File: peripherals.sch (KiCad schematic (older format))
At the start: 61 parts, among them J12 U_FL-R-SMT-1_10_, J5 U_FL-R-SMT-1_10_, J6 U_FL-R-SMT-1_10_, J7 DM3AT-SF-PEJM5, J8 693022010811, U10 NCP163ASN330T1G, U11 EMIF06-MSD02N16

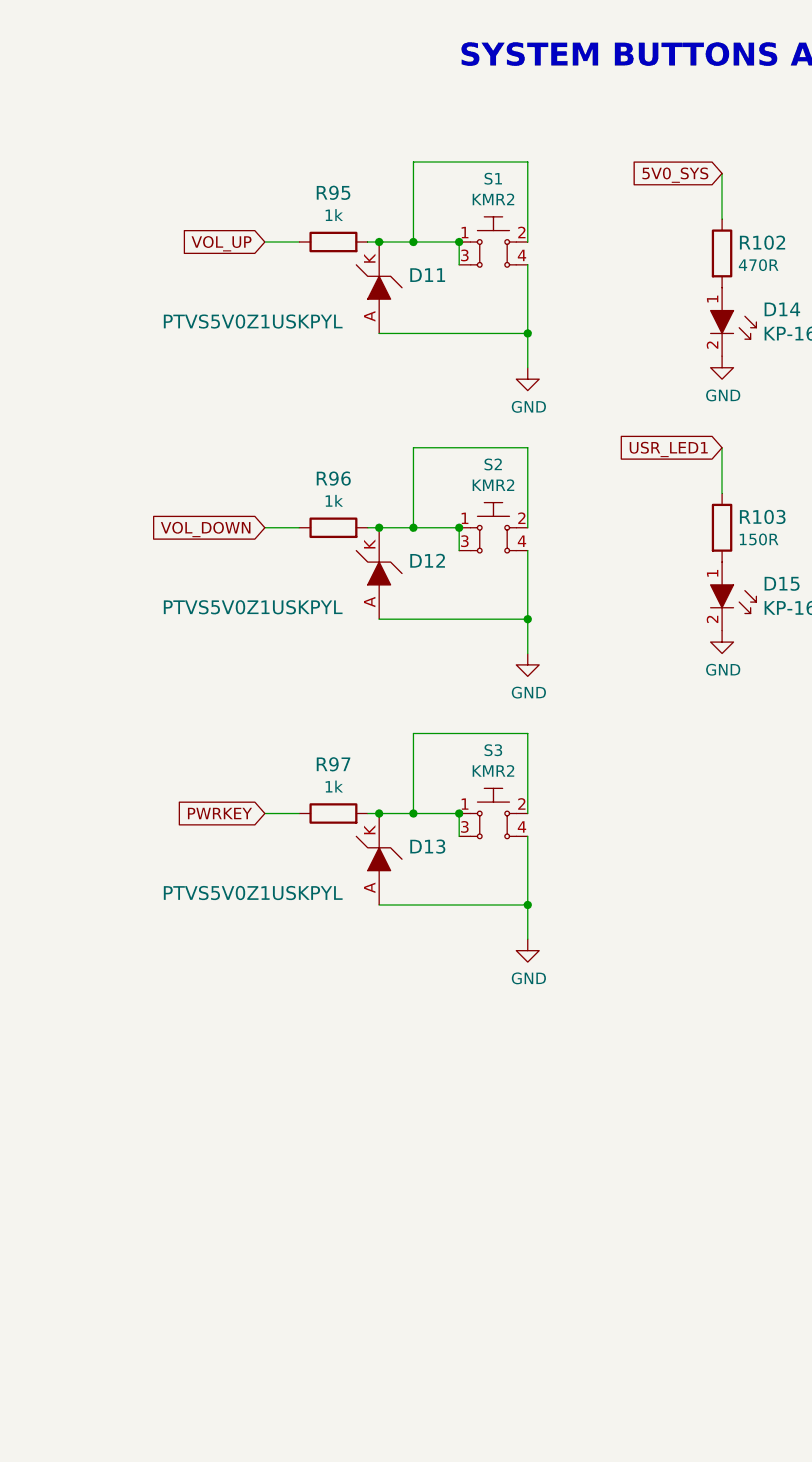
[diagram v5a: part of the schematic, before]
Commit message: Added USB BOOT, placed USR LEDs and buttons, connected Test Points
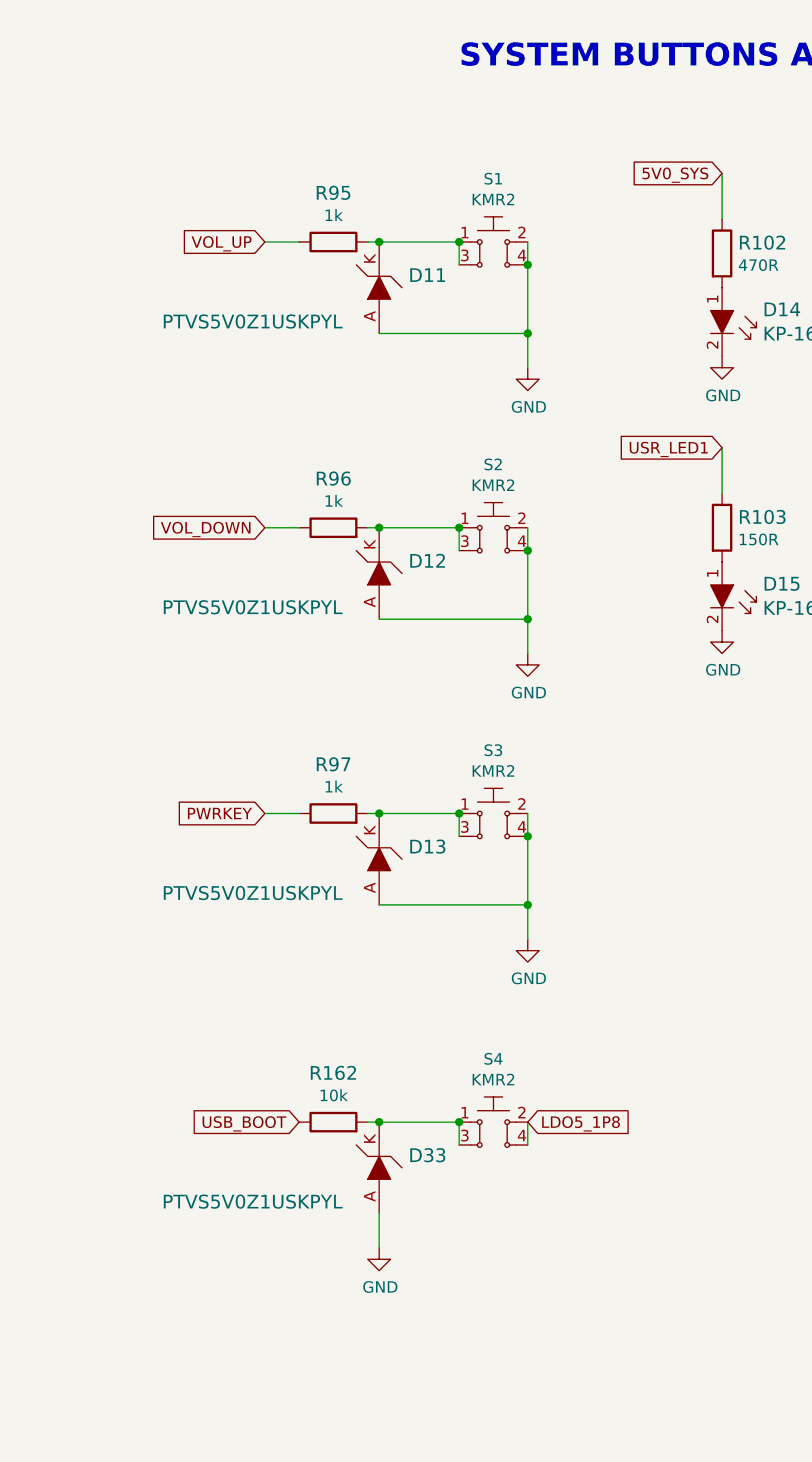
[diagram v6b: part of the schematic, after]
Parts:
- added D33: PTVS5V0Z1USKPYL, sc606-baseboard-footprints:SOD-964, symbol sc606-baseboard:PTVS5V0Z1USKPYL
- added R162: R_10k_0402, antmicro-footprints:0402-res, symbol antmicroResistors0402:R_10k_0402
- added S4: KMR2, sc606-baseboard-footprints:SW_SPST_4.2x2.8, symbol sc606-baseboard:KMR2
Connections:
- net GND: now also S1.2, S2.2, S3.2, D33.A
- net at D11.K, R95.2, S1.1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: no longer S1.2
- net at D12.K, R96.2, S2.1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: no longer S2.2
- net at D13.K, R97.2, S3.1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: no longer S3.2
- new net: D33.K, R162.2, S4.1, S4.3
- new net LDO5_1P8: S4.2, S4.4
- new net USB_BOOT: R162.1
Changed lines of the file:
@@
 VOL_UP
-$Comp
-L sc606-baseboard:KMR2 S1
-U 1 1 61E6F39D
-P 7950 5150
-F 0 "S1" H 7950 5425 50  0000 C CNN
-F 1 "KMR2" H 7950 5334 50  0000 C CNN
-F 2 "sc606-baseboard-footprints:SW_SPST_4.2x2.8" H 8150 5350 50  0001 L CNN
-F 3 "http://www.farnell.com/datasheets/2631211.pdf" H 8150 5450 60  0001 L CNN
-F 4 "KMR211NGLFS" H 8146 5543 60  0001 L CNN "MPN"
-F 5 "C&K Components" H 8150 5622 60  0001 L CNN "Manufacturer"
-	1    7950 5150
-	1    0    0    -1
-$EndComp
 $Comp
 L sc606-baseboard:GND-power #PWR0104
@@
 	1    0    0    -1
 $EndComp
-Wire Wire Line
-	7800 5150 7600 5150
-Wire Wire Line
-	8100 5150 8100 4800
-Wire Wire Line
-	8100 4800 7600 4800
-Wire Wire Line
-	7600 4800 7600 5150
-Connection ~ 7600 5150
-Wire Wire Line
-	7600 5150 7450 5150
 $Comp
 L sc606-baseboard:R_1k_0402 R95
@@
 	1    0    0    -1
 $EndComp
-Wire Wire Line
-	7800 6400 7600 6400
-Wire Wire Line
-	8100 6400 8100 6050
-Wire Wire Line
-	8100 6050 7600 6050
-Wire Wire Line
-	7600 6050 7600 6400
-Connection ~ 7600 6400
-Wire Wire Line
-	7600 6400 7450 6400
 $Comp
 L sc606-baseboard:R_1k_0402 R96
@@
 	1    0    0    -1
 $EndComp
-Wire Wire Line
-	7800 7650 7600 7650
-Wire Wire Line
-	8100 7650 8100 7300
-Wire Wire Line
-	8100 7300 7600 7300
-Wire Wire Line
-	7600 7300 7600 7650
-Connection ~ 7600 7650
-Wire Wire Line
-	7600 7650 7450 7650
 $Comp
 L sc606-baseboard:R_1k_0402 R97
@@
 Wire Wire Line
 	2600 8350 2600 8150
+Wire Wire Line
+	7450 5150 7800 5150
+$Comp
+L sc606-baseboard:KMR2 S1
+U 1 1 61E6F39D
+P 7950 5150
+F 0 "S1" H 7950 5425 50  0000 C CNN
+F 1 "KMR2" H 7950 5334 50  0000 C CNN
+F 2 "sc606-baseboard-footprints:SW_SPST_4.2x2.8" H 8150 5350 50  0001 L CNN
+F 3 "http://www.farnell.com/datasheets/2631211.pdf" H 8150 5450 60  0001 L CNN
+F 4 "KMR211NGLFS" H 8146 5543 60  0001 L CNN "MPN"
+F 5 "C&K Components" H 8150 5622 60  0001 L CNN "Manufacturer"
+	1    7950 5150
+	1    0    0    -1
+$EndComp
+Wire Wire Line
+	8100 5150 8100 5250
+Connection ~ 8100 5250
+Wire Wire Line
+	8100 6400 8100 6500
+Connection ~ 8100 6500
+Wire Wire Line
+	8100 7650 8100 7750
+Connection ~ 8100 7750
+Wire Wire Line
+	7450 7650 7800 7650
+Wire Wire Line
+	7450 6400 7800 6400
+$Comp
+L sc606-baseboard:KMR2 S4
+U 1 1 622633BF
+P 7950 9000
+F 0 "S4" H 7950 9275 50  0000 C CNN
+F 1 "KMR2" H 7950 9184 50  0000 C CNN
+F 2 "sc606-baseboard-footprints:SW_SPST_4.2x2.8" H 8150 9200 50  0001 L CNN
+F 3 "http://www.farnell.com/datasheets/2631211.pdf" H 8150 9300 60  0001 L CNN
+F 4 "KMR211NGLFS" H 8146 9393 60  0001 L CNN "MPN"
+F 5 "C&K Components" H 8150 9472 60  0001 L CNN "Manufacturer"
+	1    7950 9000
+	1    0    0    -1
+$EndComp
+$Comp
+L sc606-baseboard:PTVS5V0Z1USKPYL D33
+U 1 1 622633D6
+P 7450 9200
+F 0 "D33" V 7503 9072 60  0000 R CNN
+F 1 "PTVS5V0Z1USKPYL" V 7300 10150 60  0000 R CNN
+F 2 "sc606-baseboard-footprints:SOD-964" H 7650 9400 60  0001 L CNN
+F 3 "https://pl.mouser.com/datasheet/2/916/PTVS5V0Z1USKP-1600477.pdf" H 7650 9500 60  0001 L CNN
+F 4 "Nexperia" H 7650 10300 60  0001 L CNN "Manufacturer"
+F 5 "PTVS5V0Z1USKPYL" H 7650 9700 60  0001 L CNN "MPN"
+	1    7450 9200
+	0    -1   -1   0
+$EndComp
+Connection ~ 7450 9000
+Wire Wire Line
+	7450 9000 7400 9000
+Wire Wire Line
+	7800 9000 7800 9100
+Connection ~ 7800 9000
+Wire Wire Line
+	8100 9000 8100 9100
+Wire Wire Line
+	7450 9000 7800 9000
+Text GLabel 7100 9000 0    50   Input ~ 0
+USB_BOOT
+$Comp
+L antmicroResistors0402:R_10k_0402 R162
+U 1 1 62273D59
+P 7250 9000
+F 0 "R162" H 7250 9213 60  0000 C CNN
+F 1 "R_10k_0402" H 7250 8850 60  0001 C CNN
+F 2 "antmicro-footprints:0402-res" H 7450 9200 60  0001 L CNN
+F 3 "" H 7250 9000 50  0001 C CNN
+F 4 "VISHAY" H 7450 9400 60  0001 L CNN "Manufacturer"
+F 5 "CRCW040210K0FKEDHP" H 7450 9300 60  0001 L CNN "MPN"
+F 6 "10k" H 7250 9115 50  0000 C CNN "Val"
+	1    7250 9000
+	1    0    0    -1
+$EndComp
+Wire Wire Line
+	7450 9400 7450 9550
+$Comp
+L sc606-baseboard:GND-power #PWR0169
+U 1 1 622633C5
+P 7450 9550
+F 0 "#PWR0169" H 7450 9300 50  0001 C CNN
+F 1 "GND" H 7455 9377 50  0000 C CNN
+F 2 "" H 7450 9550 50  0001 C CNN
+F 3 "" H 7450 9550 50  0001 C CNN
+	1    7450 9550
+	1    0    0    -1
+$EndComp
 Wire Bus Line
 	700  1450 700  2150
+Text GLabel 8100 9000 2    50   Input ~ 0
+LDO5_1P8
 $EndSCHEMATC

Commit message: Started rearrangement of components. USB connectors changed to 2xUSB-C
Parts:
- added J14: CONMMCX002-SMD-T, sc606-baseboard-footprints:LINX_CONMMCX002-SMD-T, symbol sc606-baseboard:CONMMCX002-SMD-T
- R162: footprint antmicro-footprints:0402-res -> sc606-baseboard-footprints:0402-res; symbol antmicroResistors0402:R_10k_0402 -> sc606-baseboard:R_10k_0402
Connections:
- net GND: now also J14.S1, J14.S2, J14.S3, J14.S4
- net at C91.1, J12.2, R126.2: now also J14.1
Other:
- moved on the sheet: D11, D12, D13, D14, D15, D17, D18, D19, D33, R102, R103, R104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

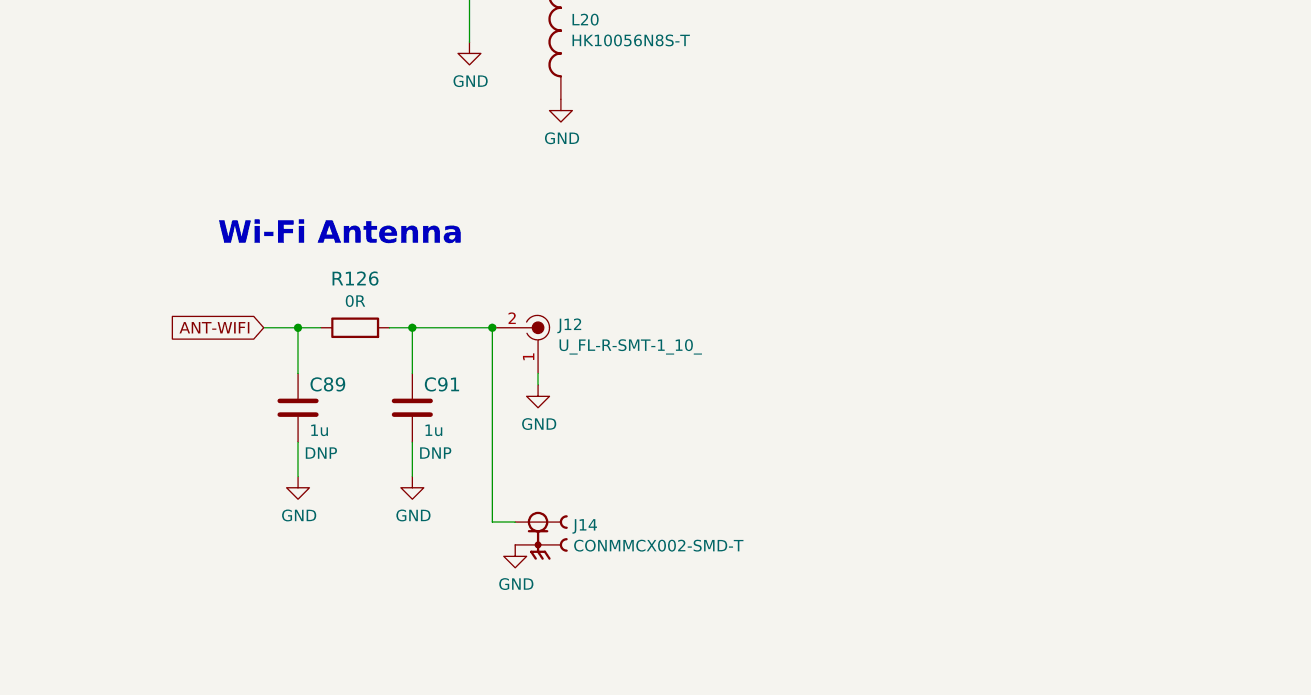
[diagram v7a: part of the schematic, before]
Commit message: All components placed on board
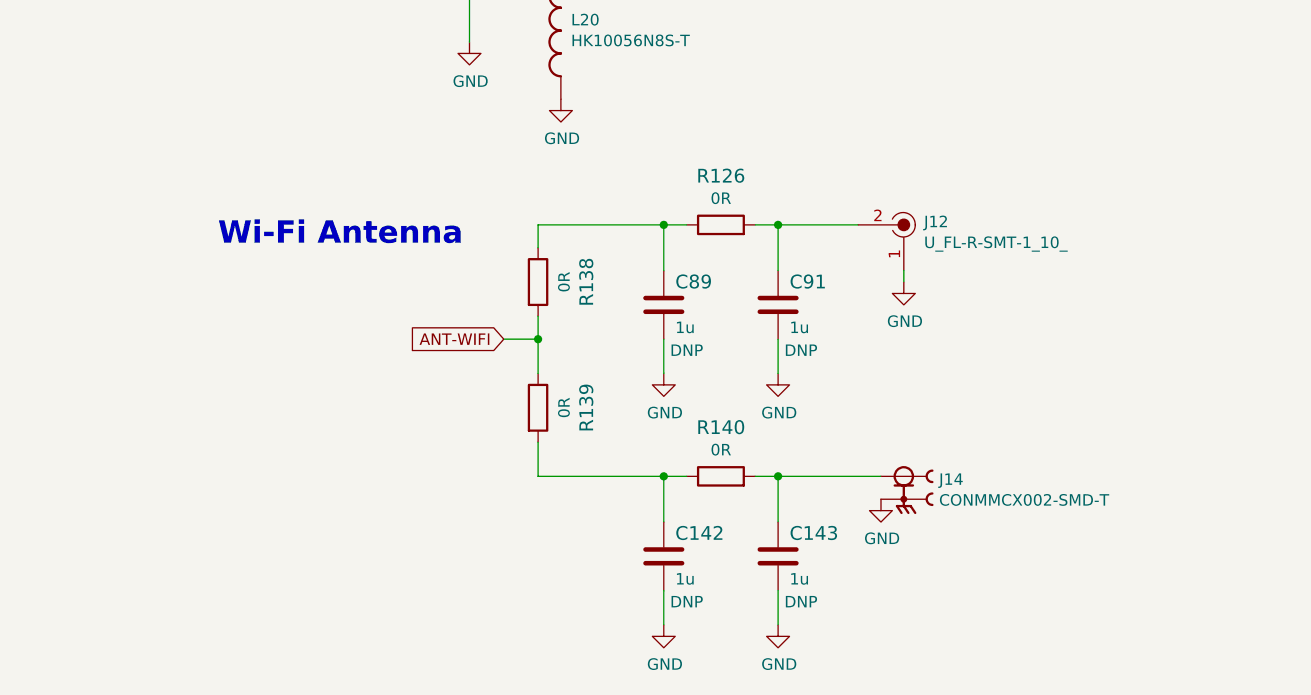
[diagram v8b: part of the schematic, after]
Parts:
- added C142, C143: C_1u_0402, sc606-baseboard-footprints:0402-cap, symbol sc606-baseboard:C_1u_0402
- added R138, R139, R140: R_0R_0402, sc606-baseboard-footprints:0402-res, symbol sc606-baseboard:R_0R_0402
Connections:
- net ANT-WIFI: now also R138.2, R139.1; no longer C89.1, R126.1
- net GND: now also C142.2, C143.2
- net at C91.1, J12.2, R126.2: no longer J14.1
- new net: C142.1, R139.2, R140.1
- new net: C143.1, J14.1, R140.2
- new net: C89.1, R126.1, R138.1
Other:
- moved on the sheet: C89, C91, J12, J14, R126
